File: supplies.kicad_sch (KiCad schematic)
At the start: 23 parts, among them U18 LMR36520, U19 LMR36520, U20 LM7812_TO220

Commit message: tweak supplies schematic
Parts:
- L3: value 33uH 3A -> 6.8uH 3A; footprint invendelirium_audio:SPM6545_horz -> (none)
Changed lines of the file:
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@@
       (effects (font (size 1.27 1.27)))
     )
-    (property "Value" "33uH 3A" (at 99.06 106.68 90)
+    (property "Value" "6.8uH 3A" (at 99.06 106.68 90)
       (effects (font (size 1.27 1.27)))
     )
-    (property "Footprint" "invendelirium_audio:SPM6545_horz" (at 99.06 107.95 0)
+    (property "Footprint" "" (at 99.06 107.95 0)
       (effects (font (size 1.27 1.27)) hide)
     )

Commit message: add dsp and esp32... schematic mostly done
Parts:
- added R6: 100, invendelirium_audio:R_0603, symbol Device:R_Small
- added U25: tps3824-50, invendelirium_general:SOT-23-5, symbol invendelirium_ic:TPS3824
- added s1: pg, invendelirium_general:pad_1.2x1.5, symbol Connector:TestPoint
- L3: value 6.8uH 3A -> 10uH 3A; footprint (none) -> invendelirium_audio:ECS_MPI4040; PN (none) -> ECS-MPI4040R2-100-R
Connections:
- net GND: now also U25.2 (gnd)
- net 3.3V renamed 5V
- net 5V: now also U25.5 (VDD)
- new net: R6.2, U25.1 (RUN)
- new net pg: R6.1, s1.1
- no-connect marks 0 -> 2
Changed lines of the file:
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@@
   (junction (at 130.81 107.95) (diameter 0) (color 0 0 0 0)
   )
+  (junction (at 191.77 124.46) (diameter 0) (color 0 0 0 0)
+  )
+  (junction (at 215.9 135.89) (diameter 0) (color 0 0 0 0)
+  )
   (junction (at 46.99 105.41) (diameter 0) (color 0 0 0 0)
   )
@@
   (junction (at 46.99 59.69) (diameter 0) (color 0 0 0 0)
   )
+  (no_connect (at 184.15 137.16))
+  (no_connect (at 199.39 139.7))
   (wire (pts (xy 85.09 105.41) (xy 85.09 99.06))
     (stroke (width 0) (type default))
@@
     (stroke (width 0) (type default))
   )
+  (wire (pts (xy 191.77 124.46) (xy 191.77 128.27))
+    (stroke (width 0) (type default))
+  )
   (wire (pts (xy 46.99 59.69) (xy 62.23 59.69))
     (stroke (width 0) (type default))
@@
     (stroke (width 0) (type default))
   )
+  (wire (pts (xy 191.77 124.46) (xy 193.04 124.46))
+    (stroke (width 0) (type default))
+  )
   (wire (pts (xy 116.84 91.44) (xy 116.84 62.23))
     (stroke (width 0) (type default))
@@
     (stroke (width 0) (type default))
   )
+  (wire (pts (xy 212.09 135.89) (xy 215.9 135.89))
+    (stroke (width 0) (type default))
+  )
   (wire (pts (xy 92.71 146.05) (xy 99.06 146.05))
     (stroke (width 0) (type default))
@@
     (stroke (width 0) (type default))
   )
+  (wire (pts (xy 199.39 135.89) (xy 207.01 135.89))
+    (stroke (width 0) (type default))
+  )
   (wire (pts (xy 72.39 120.65) (xy 74.93 120.65))
     (stroke (width 0) (type default))
   )
+  (wire (pts (xy 190.5 124.46) (xy 191.77 124.46))
+    (stroke (width 0) (type default))
+  )
   (wire (pts (xy 82.55 62.23) (xy 90.17 62.23))
     (stroke (width 0) (type default))
@@
   )
   (wire (pts (xy 105.41 68.58) (xy 105.41 69.85))
+    (stroke (width 0) (type default))
+  )
+  (wire (pts (xy 215.9 135.89) (xy 219.71 135.89))
     (stroke (width 0) (type default))
   )
@@
   (text "turn-on 7.5V" (at 48.26 46.99 90)
     (effects (font (size 1.016 1.016)) (justify right bottom))
+  )
+  (label "5V" (at 190.5 124.46 0) (fields_autoplaced)
+    (effects (font (size 1.016 1.016)) (justify left bottom))
+  )
+  (label "5V" (at 137.16 107.95 0) (fields_autoplaced)
+    (effects (font (size 1.016 1.016)) (justify left bottom))
   )
   (global_label "PVDD" (shape input) (at 34.29 59.69 180) (fields_autoplaced)
@@
     (effects (font (size 1.016 1.016)) (justify left))
   )
-  (hierarchical_label "3.3V" (shape output) (at 142.24 107.95 0) (fields_autoplaced)
+  (hierarchical_label "pg" (shape output) (at 219.71 135.89 0) (fields_autoplaced)
+    (effects (font (size 1.016 1.016)) (justify left))
+  )
+  (hierarchical_label "5V" (shape output) (at 142.24 107.95 0) (fields_autoplaced)
     (effects (font (size 1.016 1.016)) (justify left))
   )
@@
     )
   )
+  (symbol (lib_id "power:GND") (at 191.77 148.59 0) (unit 1)
+    (in_bom yes) (on_board yes) (dnp no) (fields_autoplaced)
+    (property "Reference" "#PWR02" (at 191.77 154.94 0)
+      (effects (font (size 1.27 1.27)) hide)
+    )
+    (property "Value" "GND" (at 191.77 153.67 0)
+      (effects (font (size 1.27 1.27)) hide)
+    )
+    (property "Footprint" "" (at 191.77 148.59 0)
+      (effects (font (size 1.27 1.27)) hide)
+    )
+    (property "Datasheet" "" (at 191.77 148.59 0)
+      (effects (font (size 1.27 1.27)) hide)
+    )
+    (pin "1")
+    (instances
+      (project "uberamp1"
+        (path "/310059c1-d84b-43e2-9c9a-0e426c534a12/c6ef957f-dbb4-496d-aec2-44492c2243c4"
+          (reference "#PWR02") (unit 1)
+        )
+        (path "/310059c1-d84b-43e2-9c9a-0e426c534a12/1727f815-1282-4ad8-874c-d1f66f4d7fbe"
+          (reference "#PWR070") (unit 1)
+        )
+        (path "/310059c1-d84b-43e2-9c9a-0e426c534a12/e09aca01-5377-42b6-85e8-8afbf1155690"
+          (reference "#PWR071") (unit 1)
+        )
+        (path "/310059c1-d84b-43e2-9c9a-0e426c534a12/b23c2595-3b45-43cf-b3fd-b0c94e6d7f84"
+          (reference "#PWR072") (unit 1)
+        )
+        (path "/310059c1-d84b-43e2-9c9a-0e426c534a12/4d0cf4b6-29af-402d-96b9-0bcbddb66920"
+          (reference "#PWR0159") (unit 1)
+        )
+      )
+    )
+  )
   (symbol (lib_id "power:PWR_FLAG") (at 114.3 107.95 0) (unit 1)
     (in_bom yes) (on_board yes) (dnp no) (fields_autoplaced)
@@
         (path "/310059c1-d84b-43e2-9c9a-0e426c534a12/4d0cf4b6-29af-402d-96b9-0bcbddb66920"
           (reference "#PWR0132") (unit 1)
+        )
+      )
+    )
+  )
+  (symbol (lib_id "Device:R_Small") (at 209.55 135.89 270) (unit 1)
+    (in_bom yes) (on_board yes) (dnp no) (fields_autoplaced)
+    (property "Reference" "R6" (at 209.55 130.81 90)
+      (effects (font (size 1.27 1.27)))
+    )
+    (property "Value" "100" (at 209.55 133.35 90)
+      (effects (font (size 1.27 1.27)))
+    )
+    (property "Footprint" "invendelirium_audio:R_0603" (at 209.55 135.89 0)
+      (effects (font (size 1.27 1.27)) hide)
+    )
+    (property "Datasheet" "~" (at 209.55 135.89 0)
+      (effects (font (size 1.27 1.27)) hide)
+    )
+    (pin "1")
+    (pin "2")
+    (instances
+      (project "uberamp1"
+        (path "/310059c1-d84b-43e2-9c9a-0e426c534a12/c6ef957f-dbb4-496d-aec2-44492c2243c4"
+          (reference "R6") (unit 1)
+        )
+        (path "/310059c1-d84b-43e2-9c9a-0e426c534a12/1727f815-1282-4ad8-874c-d1f66f4d7fbe"
+          (reference "R63") (unit 1)
+        )
+        (path "/310059c1-d84b-43e2-9c9a-0e426c534a12/e09aca01-5377-42b6-85e8-8afbf1155690"
+          (reference "R82") (unit 1)
+        )
+        (path "/310059c1-d84b-43e2-9c9a-0e426c534a12/b23c2595-3b45-43cf-b3fd-b0c94e6d7f84"
+          (reference "R98") (unit 1)
+        )
+        (path "/310059c1-d84b-43e2-9c9a-0e426c534a12/4d0cf4b6-29af-402d-96b9-0bcbddb66920"
+          (reference "R195") (unit 1)
         )
       )
@@
         (path "/310059c1-d84b-43e2-9c9a-0e426c534a12/4d0cf4b6-29af-402d-96b9-0bcbddb66920"
           (reference "CU18L") (unit 1)
+        )
+      )
+    )
+  )
+  (symbol (lib_id "Connector:TestPoint") (at 215.9 135.89 0) (unit 1)
+    (in_bom yes) (on_board yes) (dnp no)
+    (property "Reference" "s1" (at 214.63 128.27 0)
+      (effects (font (size 1.27 1.27)) (justify left))
+    )
+    (property "Value" "pg" (at 214.63 129.54 0)
+      (effects (font (size 1.27 1.27)) (justify left))
+    )
+    (property "Footprint" "invendelirium_general:pad_1.2x1.5" (at 220.98 135.89 0)
+      (effects (font (size 1.27 1.27)) hide)
+    )
+    (property "Datasheet" "~" (at 220.98 135.89 0)
+      (effects (font (size 1.27 1.27)) hide)
+    )
+    (pin "1")
+    (instances
+      (project "uberamp1"
+        (path "/310059c1-d84b-43e2-9c9a-0e426c534a12/c6ef957f-dbb4-496d-aec2-44492c2243c4"
+          (reference "s1") (unit 1)
+        )
+        (path "/310059c1-d84b-43e2-9c9a-0e426c534a12/1727f815-1282-4ad8-874c-d1f66f4d7fbe"
+          (reference "s3") (unit 1)
+        )
+        (path "/310059c1-d84b-43e2-9c9a-0e426c534a12/e09aca01-5377-42b6-85e8-8afbf1155690"
+          (reference "s5") (unit 1)
+        )
+        (path "/310059c1-d84b-43e2-9c9a-0e426c534a12/b23c2595-3b45-43cf-b3fd-b0c94e6d7f84"
+          (reference "s7") (unit 1)
+        )
+        (path "/310059c1-d84b-43e2-9c9a-0e426c534a12/9f0654db-0c52-4f70-8768-bb44a6ed6168"
+          (reference "s11") (unit 1)
+        )
+        (path "/310059c1-d84b-43e2-9c9a-0e426c534a12/4d0cf4b6-29af-402d-96b9-0bcbddb66920"
+          (reference "s25") (unit 1)
         )
       )
@@
       (effects (font (size 1.27 1.27)))
     )
-    (property "Value" "6.8uH 3A" (at 99.06 106.68 90)
+    (property "Value" "10uH 3A" (at 99.06 106.68 90)
       (effects (font (size 1.27 1.27)))
     )
-    (property "Footprint" "" (at 99.06 107.95 0)
+    (property "Footprint" "invendelirium_audio:ECS_MPI4040" (at 99.06 107.95 0)
       (effects (font (size 1.27 1.27)) hide)
     )
     (property "Datasheet" "~" (at 99.06 107.95 0)
       (effects (font (size 1.27 1.27)) hide)
+    )
+    (property "PN" "ECS-MPI4040R2-100-R" (at 99.06 107.95 90)
+      (effects (font (size 1.016 1.016)) hide)
     )
     (pin "1")
@@
         )
       )
+    )
+  )
+  (symbol (lib_id "invendelirium_ic:TPS3824") (at 191.77 138.43 0) (unit 1)
+    (in_bom yes) (on_board yes) (dnp no)
+    (property "Reference" "U25" (at 194.31 127 0)
+      (effects (font (size 1.27 1.27)) (justify left))
+    )
+    (property "Value" "tps3824-50" (at 199.39 129.54 0)
+      (effects (font (size 1.27 1.27)))
+    )
+    (property "Footprint" "invendelirium_general:SOT-23-5" (at 208.28 147.32 0)
+      (effects (font (size 1.27 1.27)) hide)
+    )
+    (property "Datasheet" "" (at 191.77 138.43 0)
+      (effects (font (size 1.27 1.27)) hide)
+    )
+    (pin "1")
+    (pin "2")
+    (pin "3")
+    (pin "4")
+    (pin "5")
+    (instances
+      (project "uberamp1"
+        (path "/310059c1-d84b-43e2-9c9a-0e426c534a12/4d0cf4b6-29af-402d-96b9-0bcbddb66920"
+          (reference "U25") (unit 1)
+        )
+      )

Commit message: update to kicad 8
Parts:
- renumbered C21 to C123, C14 to C124, C14 to C125, C21 to C126, C77 to C127, C77 to C132, C21 to CU18, C77 to CU18L, L3 to L10, L3 to L9, R6 to R181, R6 to R182, R6 to R183, R6 to R184, R6 to R187, R6 to R188, R6 to R195, s1 to s25

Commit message: schematic: some fixes
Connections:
- no-connect marks 2 -> 4
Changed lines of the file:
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@@
 	)
 	(junction
-		(at 116.84 146.05)
-		(diameter 0)
-		(color 0 0 0 0)
-	)
-	(junction
 		(at 99.06 146.05)
 		(diameter 0)
@@
 	)
 	(no_connect
+		(at 82.55 115.57)
+	)
+	(no_connect
+		(at 82.55 69.85)
+	)
+	(no_connect
 		(at 184.15 137.16)
 	)
@@
 	(wire
 		(pts
-			(xy 116.84 146.05) (xy 121.92 146.05)
+			(xy 110.49 146.05) (xy 121.92 146.05)
 		)
 		(stroke
@@
 	(wire
 		(pts
-			(xy 110.49 146.05) (xy 116.84 146.05)
-		)
-		(stroke
-			(width 0)
-			(type default)
-		)
-	)
-	(wire
-		(pts
 			(xy 102.87 107.95) (xy 105.41 107.95)
 		)
@@
 					(unit 1)
 				)
-			)
-		)
-	)
-	(symbol
-		(lib_id "power:PWR_FLAG")
-		(at 116.84 146.05 0)
-		(unit 1)
-		(exclude_from_sim no)
-		(in_bom yes)
-		(on_board yes)
-		(dnp no)
-		(fields_autoplaced yes)
-		(property "Reference" "#FLG09"
-			(at 116.84 144.145 0)
-			(effects
-				(font
-					(size 1.27 1.27)
-				)
-				(hide yes)
-			)
-		)
-		(property "Value" "PWR_FLAG"
-			(at 116.84 142.24 0)
-			(effects
-				(font
-					(size 1.27 1.27)
-				)
-			)
-		)
-		(property "Footprint" ""
-			(at 116.84 146.05 0)
-			(effects
-				(font
-					(size 1.27 1.27)
-				)
-				(hide yes)
-			)
-		)
-		(property "Datasheet" "~"
-			(at 116.84 146.05 0)
-			(effects
-				(font
-					(size 1.27 1.27)
-				)
-				(hide yes)
-			)
-		)
-		(property "Description" ""
-			(at 116.84 146.05 0)
-			(effects
-				(font
-					(size 1.27 1.27)
-				)
-				(hide yes)
-			)
-		)
-		(pin "1"
-		)
-		(instances
-			(project "uberamp1"
-				(path "/310059c1-d84b-43e2-9c9a-0e426c534a12/4d0cf4b6-29af-402d-96b9-0bcbddb66920"
-					(reference "#FLG09")
-					(unit 1)
-				)

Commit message: updates
* add line out
* fix almost all erc
* some more random edits
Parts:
- U25: PN (none) -> tps3824-50
- renumbered C127 to CU19L, C132 to CU20
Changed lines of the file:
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@@
 		(on_board yes)
 		(dnp no)
-		(property "Reference" "C132"
+		(property "Reference" "CU20"
 			(at 100.33 147.32 0)
 			(effects
@@
 			(project "uberamp1"
 				(path "/310059c1-d84b-43e2-9c9a-0e426c534a12/4d0cf4b6-29af-402d-96b9-0bcbddb66920"
-					(reference "C132")
+					(reference "CU20")
 					(unit 1)
 				)
@@
 			)
 		)
+		(property "PN" "tps3824-50"
+			(at 191.77 138.43 0)
+			(effects
+				(font
+					(size 1.27 1.27)
+				)
+				(hide yes)
+			)
+		)
 		(pin "1"
 		)
@@
 		(on_board yes)
 		(dnp no)
-		(property "Reference" "C127"
+		(property "Reference" "CU19L"
 			(at 121.92 109.22 0)
 			(effects
@@
 			(project "uberamp1"
 				(path "/310059c1-d84b-43e2-9c9a-0e426c534a12/4d0cf4b6-29af-402d-96b9-0bcbddb66920"
-					(reference "C127")
-					(unit 1)
-				)
+					(reference "CU19L")
+					(unit 1)
+				)

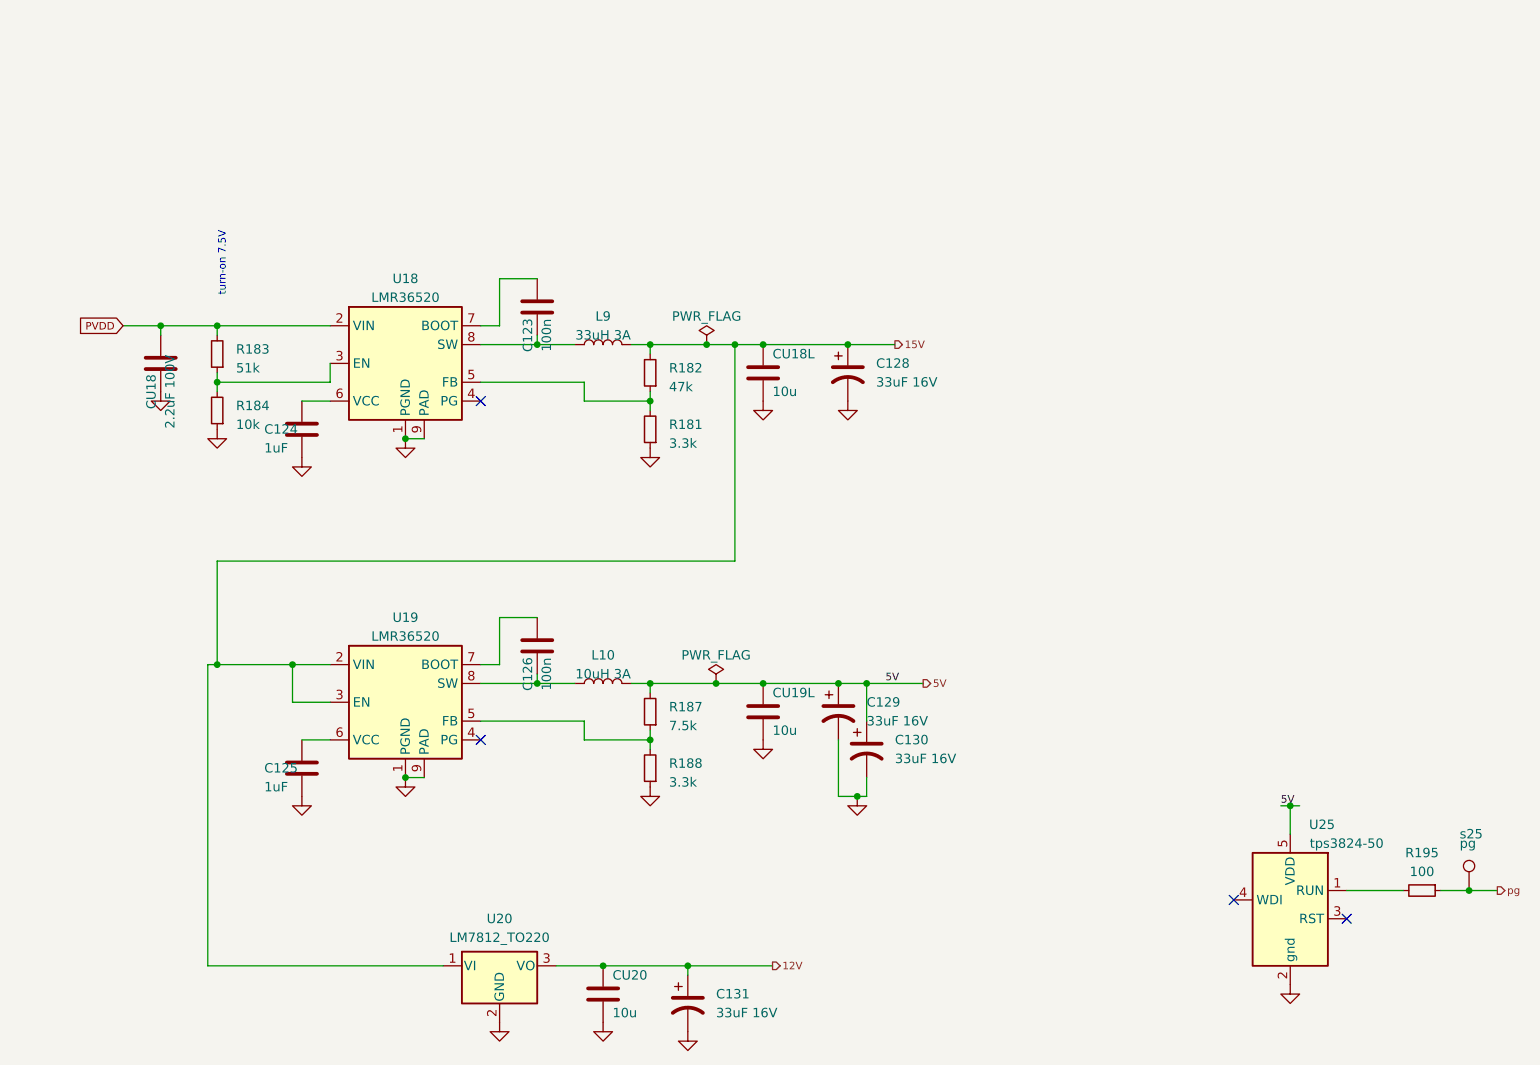
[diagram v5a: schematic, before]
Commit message: add power input +...
+ tons of fixes, footprint assignments, etc
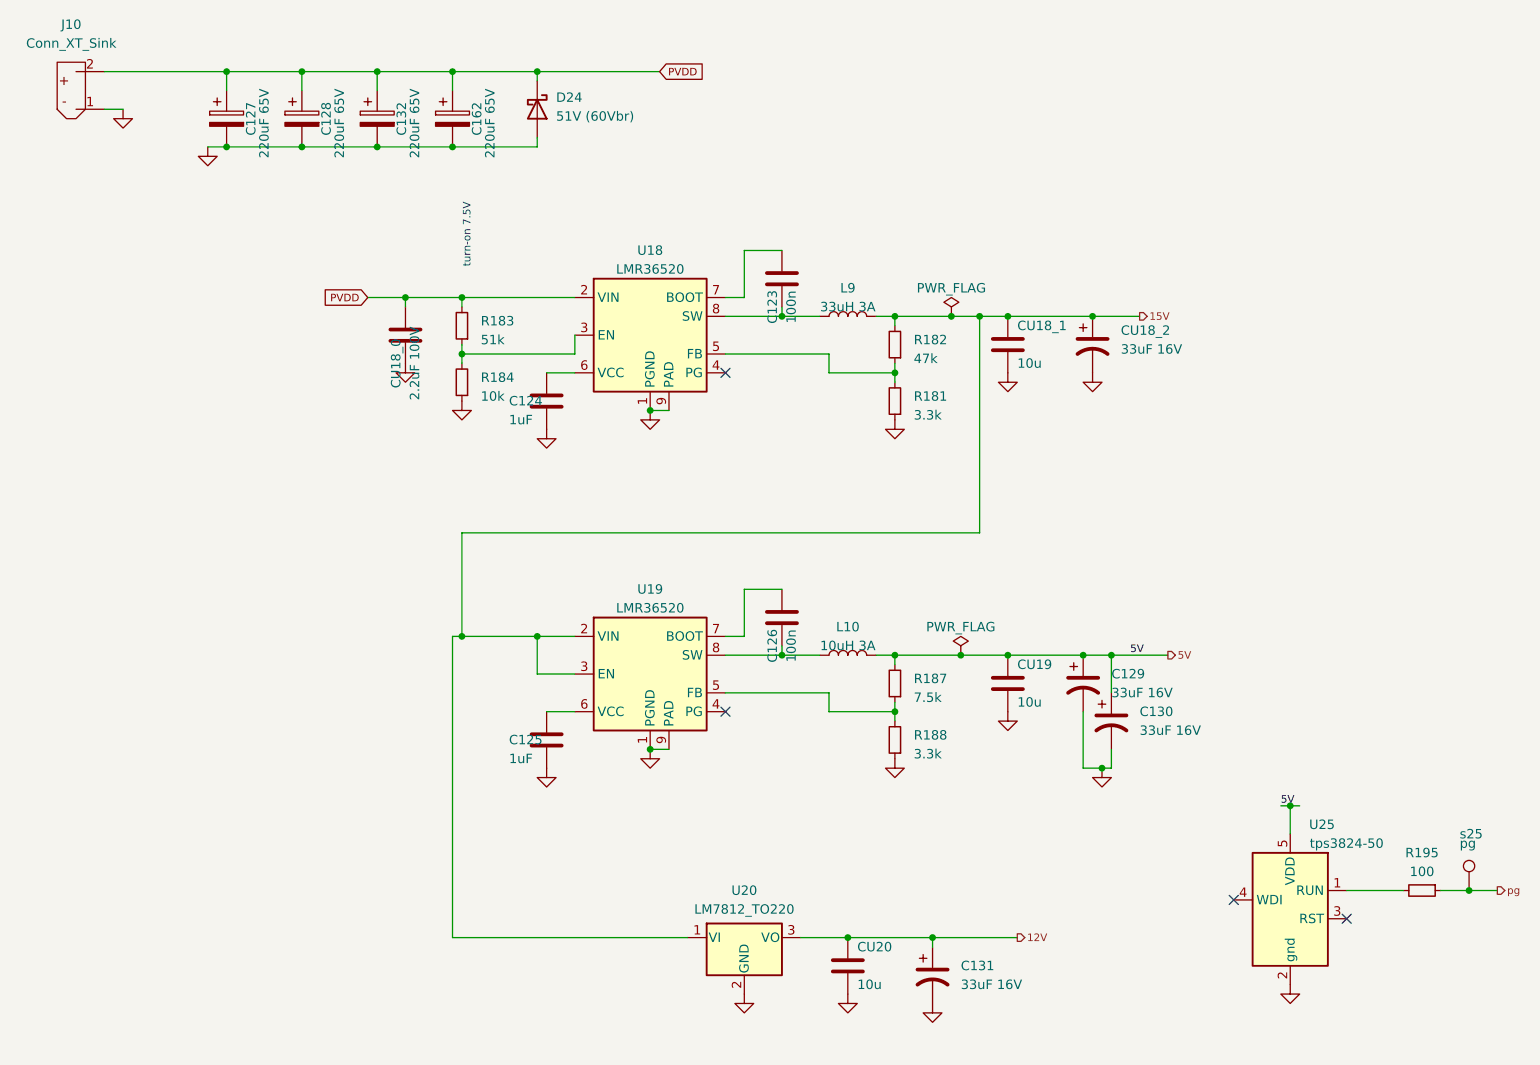
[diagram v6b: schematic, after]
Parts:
- added C127, C128, C132, C162: 220uF 65V, Capacitor_THT:CP_Radial_D12.5mm_P5.00mm, symbol Device:C_Polarized
- added D24: 51V (60Vbr), Diode_SMD:D_SMB, symbol Device:D_Schottky
- added J10: Conn_XT_Sink, Connector_AMASS:AMASS_XT30U-M_1x02_P5.0mm_Vertical, symbol victor_strawlab:Conn_XT_Sink
- U18, U19: PN (none) -> LMR36520
- U20: PN (none) -> L7812CV
- renumbered CU18 to CU18_0, CU18L to CU18_1, C128 to CU18_2, CU19L to CU19
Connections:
- net GND: now also C127.2, C128.2, C132.2, C162.2, D24.2 (A), J10.1 (minus1)
- net PVDD: now also C127.1, C128.1, C132.1, C162.1, D24.1 (K), J10.2 (plus)
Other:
- moved on the sheet: C123, C124, C125, C126, C129, C130, C131, CU18_0, CU18_1, CU18_2, CU19, CU20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
